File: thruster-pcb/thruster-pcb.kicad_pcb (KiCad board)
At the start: 4 copper layers, 40 x 40 mm, 103 parts, among them J1301 Connector_USB_C_Receptacle, J301 Molex_Pico-SPOX_Horizontal, J302 Molex_Pico-Lock-PLUS_Vertical, J401 Molex_Pico-SPOX_Horizontal, J402 Molex_Pico-Clasp_Horizontal, M301 Fan_5VDC_25x25x8mm, Q301 MOSFET-N-CH, SW1301 Switch_Tactile_SPST-NO_SMT_Si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, U1001 BUK7D36-60EX, U1101 BUK7D36-60EX, U1201 BUK7D36-60EX, U1301 Linear_3.3V_1A, U1302 MCU_RP2040, U1303 Memory_Flash_W25Q128JVZPIQ, U301 Switching_5V_500mA, U302 Linear_3.3V_1A, U401 TMC5160A-WA, U402 MAX6816, U501 BUK7D36-60EX, U601 BUK7D36-60EX, U701 BUK7D36-60EX, U801 BUK7D36-60EX, U901 BUK7D36-60EX, X401 16MHz, Y1301 Crystal_12MHz

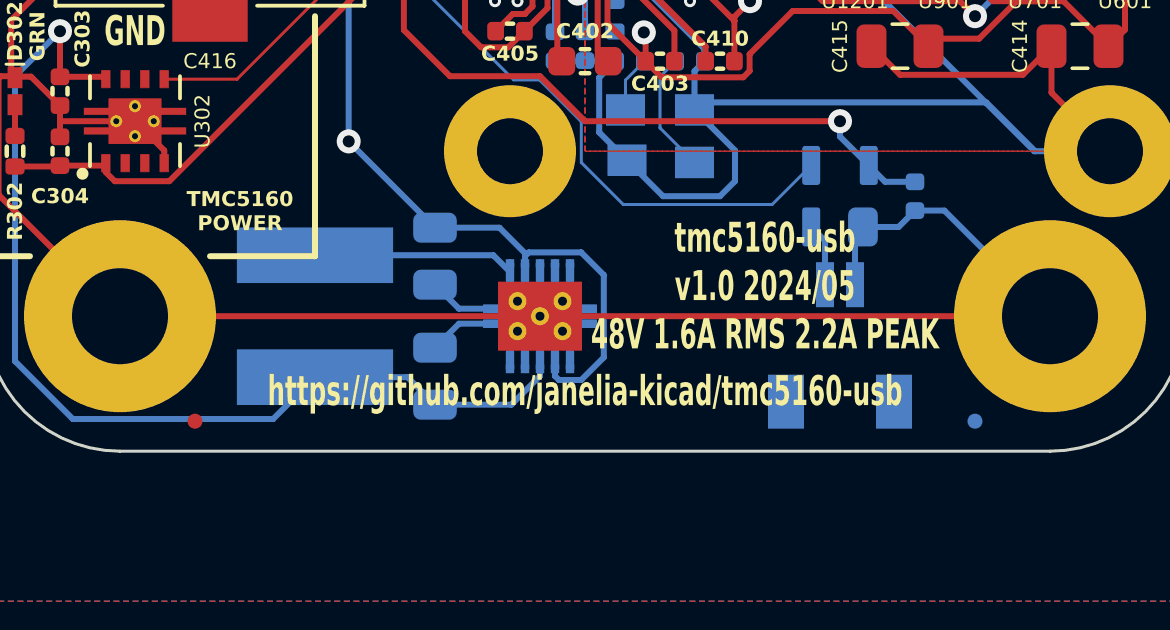
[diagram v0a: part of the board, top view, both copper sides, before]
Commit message: tmc5160-usb -> thruster-pcb
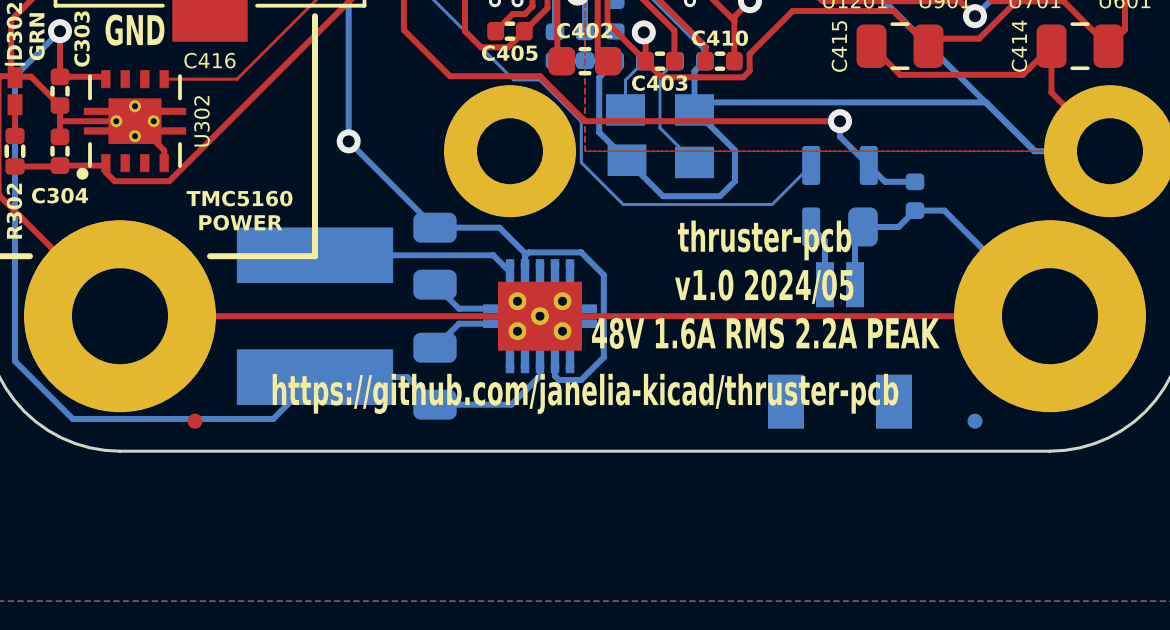
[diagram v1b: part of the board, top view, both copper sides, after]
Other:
- board text added: "https://github.com/janelia-kicad/thruster-pcb"
- board text added: "thruster-pcb v1.0 2024/05 48V 1.6A RMS 2.2A PEAK"
- board text removed: "https://github.com/janelia-kicad/tmc5160-usb"
- board text removed: "tmc5160-usb v1.0 2024/05 48V 1.6A RMS 2.2A PEAK"
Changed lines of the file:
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@@
   (paper "A4")
   (title_block
-    (title "tmc5160-usb")
+    (title "thruster-pcb")
     (date "2024-05-08")
     (rev "1.0")
@@
     (effects (font (size 1 0.6) (thickness 0.15) bold))
   )
-  (gr_text "tmc5160-usb\nv1.0 2024/05\n48V 1.6A RMS 2.2A PEAK" (at 158.4 116.1) (layer "F.SilkS")
+  (gr_text "thruster-pcb\nv1.0 2024/05\n48V 1.6A RMS 2.2A PEAK" (at 158.4 116.1) (layer "F.SilkS")
     (effects (font (size 1 0.6) (thickness 0.15) bold))
   )
-  (gr_text "https://github.com/janelia-kicad/tmc5160-usb" (at 152.4 119.6) (layer "F.SilkS")
+  (gr_text "https://github.com/janelia-kicad/thruster-pcb" (at 152.4 119.6) (layer "F.SilkS")
     (effects (font (size 1 0.6) (thickness 0.15) bold))
   )

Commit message: Add reference files
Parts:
- removed C1301, C1302, C303, C304, C305: 1uF_25V, Janelia:C_0402_1005Metric
- removed C1303, C1311: 1uF_35V, Janelia:C_0402_1005Metric
- removed C1304, C1305, C1306, C1307, C1308, C1309, C1310, C1312, C1313, C1314, C401, C403, C404, C408, C413, C417: 0.1uF_100V, Janelia:C_0402_1005Metric
- removed C1315, C1316: 15pF_25V, Janelia:C_0402_1005Metric
- removed C301, C414, C415: 2.2uF_100V, Janelia:C_0805_2012Metric
- removed C302: 47uF_10V, Janelia:C_0805_2012Metric
- removed C402: 22nF_100V, Janelia:C_0603_1608Metric
- removed C405: 0.47uF_35V, Janelia:C_0402_1005Metric
- removed C406, C407: 2.2uF_35V, Janelia:C_0402_1005Metric
- removed C409, C410, C411, C412: 0.22uF_25V, Janelia:C_0402_1005Metric
- removed C416: 220uF_63V, Janelia:CP_Hybrid_EEHZS1H221V
- removed D1301, D1302: D_SCHOTTKY_40V_2A, Janelia:CR_DSN2_152AB-C_OSI
- removed D301: LED_RED, Janelia:LED_0402-1005_KNB
- removed D302: LED_GRN, Janelia:LED_0402-1005_KNB
- removed D303: LED_YEL, Janelia:LED_0402-1005_KNB
- removed D401: D_Zener_48V_2.6A, Janelia:SMFSeries_LTF
- removed FID201, FID202, FID203, FID204: FIDUCIAL_0.5mm_MASK1mm, Janelia:FIDUCIAL_0.5mm_Mask1mm
- removed H201, H202, H203, H204: MountingHole_M3_Pad, Janelia:MountingHole_3.2mm_M3_Pad
- removed J1301: Connector_USB_C_Receptacle, Janelia:USB_C_Receptacle_Amphenol_10152803-00011LF
- removed J301: Molex_Pico-SPOX_Horizontal, Janelia:Molex_Pico-SPOX-87438_1x02-P1.5mm_Horizontal
- removed J302: Molex_Pico-Lock-PLUS_Vertical, Janelia:Molex_Micro-Lock-PLUS-505568_1x02_P1.25mm_Vertical
- removed J401: Molex_Pico-SPOX_Horizontal, Janelia:Molex_Pico-SPOX-87438_1x04-P1.5mm_Horizontal
- removed J402: Molex_Pico-Clasp_Horizontal, Janelia:Molex_Pico-Clasp-501568_1x02_P1mm_Horizontal
- removed L301: 150uH_553mA, Janelia:IND_CB_SD25
- removed M301: Fan_5VDC_25x25x8mm, Janelia:FAN_5VDC_25x25x8mm
- removed Q301: MOSFET-N-CH, Janelia:XFDFN-3
- removed R1001, R1101, R1201, R501, R601, R701, R801, R901: 15, Janelia:R_0402_1005Metric
- removed R1301: 10.0k, Janelia:R_0402_1005Metric
- removed R1302, R1303: 5.1k, Janelia:R_0402_1005Metric
- removed R1304, R1305: 27, Janelia:R_0402_1005Metric
- removed R1306, R1307: 1k, Janelia:R_0402_1005Metric
- removed R301: 2.32k, Janelia:R_0805_2012Metric
- removed R302: 64.9, Janelia:R_0402_1005Metric
- removed R303: 249, Janelia:R_0402_1005Metric
- removed R401: 2.2, Janelia:R_0402_1005Metric
- removed R402, R403, R406, R407: 47, Janelia:R_0402_1005Metric
- removed R404, R405: 0.15, Janelia:R_1206_3216Metric
- removed SW1301: Switch_Tactile_SPST-NO_SMT_Side, Janelia:SMT_1045822_WRE
- removed U1001, U1101, U1201, U501, U601, U701, U801, U901: BUK7D36-60EX, Janelia:BUK7D3660EX_NEX
- removed U1301, U302: Linear_3.3V_1A, Janelia:TPS737Q1
- removed U1302: MCU_RP2040, Janelia:QFN-56-1EP_7x7mm_P0.4mm_EP3.2x3.2mm
- removed U1303: Memory_Flash_W25Q128JVZPIQ, Janelia:WSON-8-1EP_6x5mm_P1.27mm_EP3.4x4.3mm
- removed U301: Switching_5V_500mA, Janelia:Texas_S-PVSON-N10_ThermalVias
- removed U401: TMC5160A-WA, Janelia:21-100593_ADI
- removed U402: MAX6816, Janelia:SOT192P237X122-4N
- removed X401: 16MHz, Janelia:OSC_ECS-2520S33-160-FN-TR
- removed Y1301: Crystal_12MHz, Janelia:Crystal_SMD_Abracon_ABM8-4Pin_3.2x2.5mm
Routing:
- net /GND: track 474.9 -> 0.00 mm, vias 6 -> 0
- net /VM: track 133.3 -> 0.00 mm, vias 4 -> 0
- net /rp2040/+3.3V: track 87.1 -> 0.00 mm, vias 4 -> 0
- net /+5V: track 81.3 -> 0.00 mm, vias 3 -> 0
- net /VIO: track 56.5 -> 0.00 mm, vias 1 -> 0
- net /tmc5160/BMA1: track 39.3 -> 0.00 mm, vias 2 -> 0
- net /tmc5160/SRA: track 37.6 -> 0.00 mm
- net /tmc5160/BMB2: track 33.1 -> 0.00 mm, vias 2 -> 0
- net /tmc5160/BMA2: track 32.7 -> 0.00 mm, vias 3 -> 0
- net /tmc5160/SRB: track 32.5 -> 0.00 mm
- net /tmc5160/REFL_DEBOUNCED: track 28.1 -> 0.00 mm, vias 1 -> 0
- net /tmc5160/BMB1: track 27.4 -> 0.00 mm, vias 2 -> 0
- net /tmc5160/VCC: track 21.8 -> 0.00 mm, vias 2 -> 0
- net /rp2040/+1.1V: track 20.7 -> 0.00 mm
- net /tmc5160/LA1: track 20.6 -> 0.00 mm, vias 2 -> 0
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- removed copper zone on B.Cu, net /GND
- removed copper zone on F.Cu, net /GND
- removed copper zone on In1.Cu, net /GND
- removed copper zone on F.Cu, net /VM
- removed copper zone on In2.Cu, net /VM
- removed copper zone on B.Cu, net /rp2040/+1.1V
- removed copper zone on B.Cu, net /rp2040/+3.3V
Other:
- board text removed: "+"
- board text removed: "-"
- board text removed: "48V"
- board text removed: "A1"
- board text removed: "A2"
- board text removed: "B1"
- board text removed: "B2"
- board text removed: "BOOTSEL"
- board text removed: "FAN"
- board text removed: "GND"
- board text removed: "GRN"
- board text removed: "Molex 0874380243"
- board text removed: "Molex 0874380443"
- board text removed: "Molex 5015680207"
- board text removed: "Molex 5055680281 Fan 255M"
- board text removed: "RED"
- board text removed: "REFL"
- board text removed: "TMC5160 POWER"
- board text removed: "USB-C"
- board text removed: "YEL"
- board text removed: "https://github.com/janelia-kicad/thruster-pcb"
- board text removed: "thruster-pcb v1.0 2024/05 48V 1.6A RMS 2.2A PEAK"

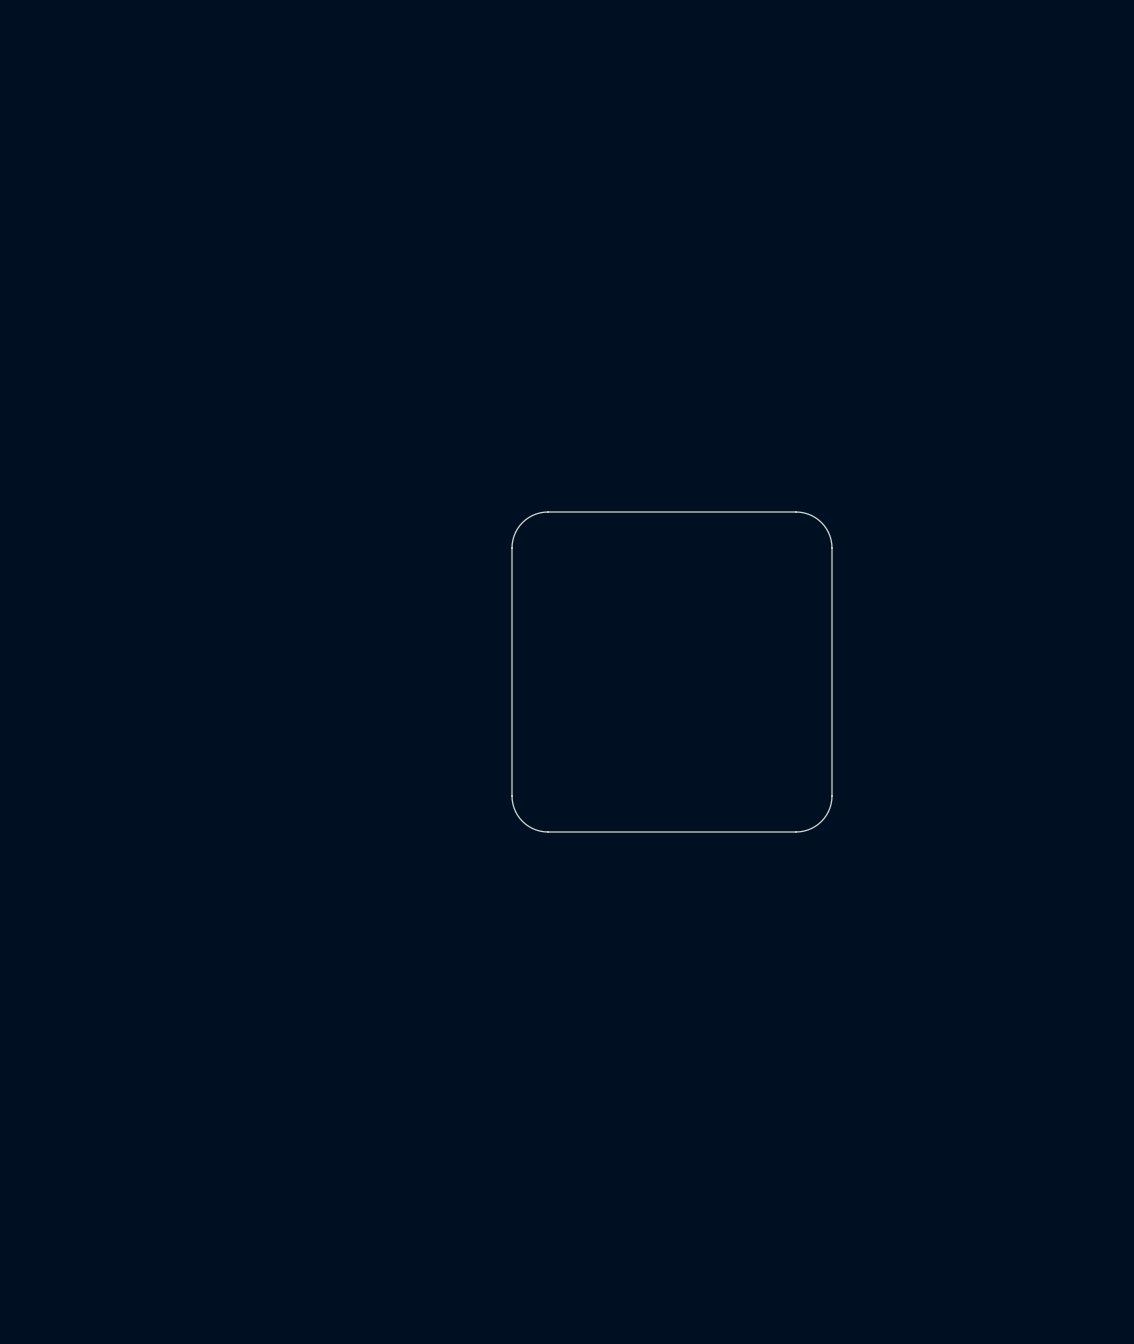
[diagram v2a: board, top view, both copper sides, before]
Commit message: Use PCA9685 and nRF52
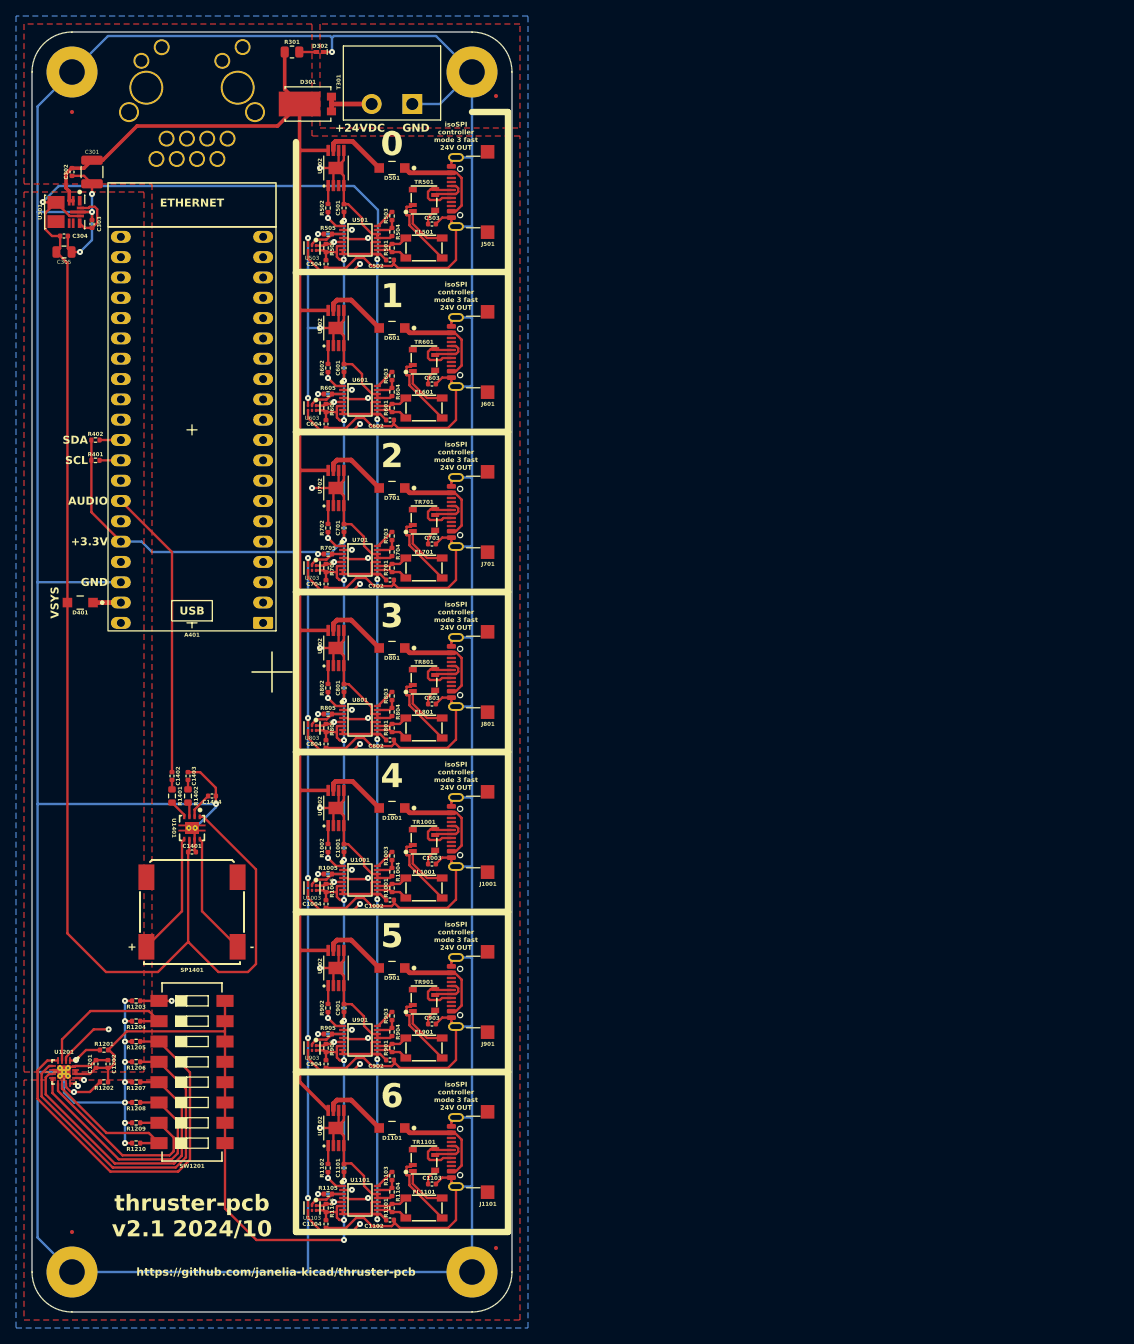
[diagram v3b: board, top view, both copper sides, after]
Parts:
- added A401: PICO_W5500_EVB, Janelia:Pico-W5500-EVB_Header_Holes, F.Cu at (92.4, 95.5)
- added C1001: 0.1uF_100V, Janelia:C_0402_1005Metric, F.Cu at (111.4, 123.6)
- added C1002: 0.1uF_100V, Janelia:C_0402_1005Metric, F.Cu at (117.2, 130.1)
- added C1003: 27pF_50V, Janelia:C_0402_1005Metric, F.Cu at (122.4, 125.6)
- added C1004: 0.1uF_100V, Janelia:C_0402_1005Metric, F.Cu at (109.2, 130.6)
- added C1101: 0.1uF_100V, Janelia:C_0402_1005Metric, F.Cu at (111.4, 163.6)
- added C1102: 0.1uF_100V, Janelia:C_0402_1005Metric, F.Cu at (117.2, 170.1)
- added C1103: 27pF_50V, Janelia:C_0402_1005Metric, F.Cu at (122.4, 165.6)
- added C1104: 0.1uF_100V, Janelia:C_0402_1005Metric, F.Cu at (109.2, 170.6)
- added C1201: 0.1uF_100V, Janelia:C_0402_1005Metric, F.Cu at (80.4, 150.6)
- added C1202: 0.1uF_100V, Janelia:C_0402_1005Metric, F.Cu at (81.9, 150.6)
- added C1401: 1uF_35V, Janelia:C_0402_1005Metric, F.Cu at (92.4, 124.1)
- added C1402: 0.22uF_25V, Janelia:C_0402_1005Metric, F.Cu at (89.9, 114.6)
- added C1403: 0.22uF_25V, Janelia:C_0402_1005Metric, F.Cu at (91.9, 114.6)
- added C1404: 0.22uF_25V, Janelia:C_0402_1005Metric, F.Cu at (94.9, 117.1)
- added C301: 3.3uF_50V, Janelia:C_1210_3225Metric, F.Cu at (79.9, 39.1)
- added C302: 0.1uF_100V, Janelia:C_0402_1005Metric, F.Cu at (77.4, 39.1)
- added C303: 1uF_25V, Janelia:C_0402_1005Metric, F.Cu at (79.9, 45.6)
- added C304: 1uF_25V, Janelia:C_0402_1005Metric, F.Cu at (76.4, 47.1)
- added C305: 47uF_10V, Janelia:C_0805_2012Metric, F.Cu at (76.4, 49.1)
- added C501: 0.1uF_100V, Janelia:C_0402_1005Metric, F.Cu at (111.4, 43.6)
- added C502: 0.1uF_100V, Janelia:C_0402_1005Metric, F.Cu at (117.2, 50.1)
- added C503: 27pF_50V, Janelia:C_0402_1005Metric, F.Cu at (122.4, 45.6)
- added C504: 0.1uF_100V, Janelia:C_0402_1005Metric, F.Cu at (109.2, 50.6)
- added C601: 0.1uF_100V, Janelia:C_0402_1005Metric, F.Cu at (111.4, 63.6)
- added C602: 0.1uF_100V, Janelia:C_0402_1005Metric, F.Cu at (117.2, 70.1)
- added C603: 27pF_50V, Janelia:C_0402_1005Metric, F.Cu at (122.4, 65.6)
- added C604: 0.1uF_100V, Janelia:C_0402_1005Metric, F.Cu at (109.2, 70.6)
- added C701: 0.1uF_100V, Janelia:C_0402_1005Metric, F.Cu at (111.4, 83.6)
- added C702: 0.1uF_100V, Janelia:C_0402_1005Metric, F.Cu at (117.2, 90.1)
- added C703: 27pF_50V, Janelia:C_0402_1005Metric, F.Cu at (122.4, 85.6)
- added C704: 0.1uF_100V, Janelia:C_0402_1005Metric, F.Cu at (109.2, 90.6)
- added C801: 0.1uF_100V, Janelia:C_0402_1005Metric, F.Cu at (111.4, 103.6)
- added C802: 0.1uF_100V, Janelia:C_0402_1005Metric, F.Cu at (117.2, 110.1)
- added C803: 27pF_50V, Janelia:C_0402_1005Metric, F.Cu at (122.4, 105.6)
- added C804: 0.1uF_100V, Janelia:C_0402_1005Metric, F.Cu at (109.2, 110.6)
- added C901: 0.1uF_100V, Janelia:C_0402_1005Metric, F.Cu at (111.4, 143.6)
- added C902: 0.1uF_100V, Janelia:C_0402_1005Metric, F.Cu at (117.2, 150.1)
- added C903: 27pF_50V, Janelia:C_0402_1005Metric, F.Cu at (122.4, 145.6)
- added C904: 0.1uF_100V, Janelia:C_0402_1005Metric, F.Cu at (109.2, 150.6)
- added D1001: D_SCHOTTKY_20V_1A, Janelia:SOD-123FL, F.Cu at (117.4, 118.6)
- added D1101: D_SCHOTTKY_20V_1A, Janelia:SOD-123FL, F.Cu at (117.4, 158.6)
- added D301: D_50V_15A, Janelia:POWERDI5_DIO, F.Cu at (106.9, 30.6)
- added D302: LED_RED, Janelia:LED_0402-1005_KNB, F.Cu at (108.4, 24.1)
- added D401: D_SCHOTTKY_20V_1A, Janelia:SOD-123FL, F.Cu at (78.4, 92.9)
- added D501: D_SCHOTTKY_20V_1A, Janelia:SOD-123FL, F.Cu at (117.4, 38.6)
- added D601: D_SCHOTTKY_20V_1A, Janelia:SOD-123FL, F.Cu at (117.4, 58.6)
- added D701: D_SCHOTTKY_20V_1A, Janelia:SOD-123FL, F.Cu at (117.4, 78.6)
- added D801: D_SCHOTTKY_20V_1A, Janelia:SOD-123FL, F.Cu at (117.4, 98.6)
- added D901: D_SCHOTTKY_20V_1A, Janelia:SOD-123FL, F.Cu at (117.4, 138.6)
- added FID201: FIDUCIAL_0.5mm_MASK1mm, Janelia:FIDUCIAL_0.5mm_Mask1mm, F.Cu at (77.4, 31.6)
- added FID202: FIDUCIAL_0.5mm_MASK1mm, Janelia:FIDUCIAL_0.5mm_Mask1mm, F.Cu at (130.4, 29.6)
- added FID203: FIDUCIAL_0.5mm_MASK1mm, Janelia:FIDUCIAL_0.5mm_Mask1mm, F.Cu at (130.4, 173.6)
- added FID204: FIDUCIAL_0.5mm_MASK1mm, Janelia:FIDUCIAL_0.5mm_Mask1mm, F.Cu at (77.4, 171.6)
- added FL1001: Choke_CMF_ACT45B-220-2P, Janelia:SMD_0-2P-TL003_TDK-L, F.Cu at (121.4, 128.6)
- added FL1101: Choke_CMF_ACT45B-220-2P, Janelia:SMD_0-2P-TL003_TDK-L, F.Cu at (121.4, 168.6)
- added FL501: Choke_CMF_ACT45B-220-2P, Janelia:SMD_0-2P-TL003_TDK-L, F.Cu at (121.4, 48.6)
- added FL601: Choke_CMF_ACT45B-220-2P, Janelia:SMD_0-2P-TL003_TDK-L, F.Cu at (121.4, 68.6)
- added FL701: Choke_CMF_ACT45B-220-2P, Janelia:SMD_0-2P-TL003_TDK-L, F.Cu at (121.4, 88.6)
- added FL801: Choke_CMF_ACT45B-220-2P, Janelia:SMD_0-2P-TL003_TDK-L, F.Cu at (121.4, 108.6)
- added FL901: Choke_CMF_ACT45B-220-2P, Janelia:SMD_0-2P-TL003_TDK-L, F.Cu at (121.4, 148.6)
- added H201: MountingHole_M3_Pad, Janelia:MountingHole_3.2mm_M3_Pad, F.Cu at (77.4, 26.6)
- added H202: MountingHole_M3_Pad, Janelia:MountingHole_3.2mm_M3_Pad, F.Cu at (127.4, 26.6)
- added H203: MountingHole_M3_Pad, Janelia:MountingHole_3.2mm_M3_Pad, F.Cu at (127.4, 176.6)
- added H204: MountingHole_M3_Pad, Janelia:MountingHole_3.2mm_M3_Pad, F.Cu at (77.4, 176.6)
- added J1001: Connector_USB_C_Receptacle_USB2.0_16P_GT-USB-7047C, Janelia:USB_C_Receptacle_GT-USB-7047C_16P_TopMnt_Horizontal, F.Cu at (125.4, 121.6)
- added J1101: Connector_USB_C_Receptacle_USB2.0_16P_GT-USB-7047C, Janelia:USB_C_Receptacle_GT-USB-7047C_16P_TopMnt_Horizontal, F.Cu at (125.4, 161.6)
- added J501: Connector_USB_C_Receptacle_USB2.0_16P_GT-USB-7047C, Janelia:USB_C_Receptacle_GT-USB-7047C_16P_TopMnt_Horizontal, F.Cu at (125.4, 41.6)
- added J601: Connector_USB_C_Receptacle_USB2.0_16P_GT-USB-7047C, Janelia:USB_C_Receptacle_GT-USB-7047C_16P_TopMnt_Horizontal, F.Cu at (125.4, 61.6)
- added J701: Connector_USB_C_Receptacle_USB2.0_16P_GT-USB-7047C, Janelia:USB_C_Receptacle_GT-USB-7047C_16P_TopMnt_Horizontal, F.Cu at (125.4, 81.6)
- added J801: Connector_USB_C_Receptacle_USB2.0_16P_GT-USB-7047C, Janelia:USB_C_Receptacle_GT-USB-7047C_16P_TopMnt_Horizontal, F.Cu at (125.4, 101.6)
- added J901: Connector_USB_C_Receptacle_USB2.0_16P_GT-USB-7047C, Janelia:USB_C_Receptacle_GT-USB-7047C_16P_TopMnt_Horizontal, F.Cu at (125.4, 141.6)
- added R1001: 100, Janelia:R_0402_1005Metric, F.Cu at (117.4, 128.6)
- added R1002: 4.7k, Janelia:R_0402_1005Metric, F.Cu at (109.4, 123.6)
- added R1003: 1.4k, Janelia:R_0402_1005Metric, F.Cu at (117.4, 124.6)
- added R1004: 604, Janelia:R_0402_1005Metric, F.Cu at (117.4, 126.6)
- added R1005: 1.8k, Janelia:R_0402_1005Metric, F.Cu at (109.4, 126.8)
- added R1006: 1.8k, Janelia:R_0402_1005Metric, F.Cu at (109.2, 128.6)
- added R1101: 100, Janelia:R_0402_1005Metric, F.Cu at (117.4, 168.6)
- added R1102: 4.7k, Janelia:R_0402_1005Metric, F.Cu at (109.4, 163.6)
- added R1103: 1.4k, Janelia:R_0402_1005Metric, F.Cu at (117.4, 164.6)
- added R1104: 604, Janelia:R_0402_1005Metric, F.Cu at (117.4, 166.6)
- added R1105: 1.8k, Janelia:R_0402_1005Metric, F.Cu at (109.4, 166.8)
- added R1106: 1.8k, Janelia:R_0402_1005Metric, F.Cu at (109.2, 168.6)
- added R1201: 10.0k, Janelia:R_0402_1005Metric, F.Cu at (81.4, 148.8)
- added R1202: 10.0k, Janelia:R_0402_1005Metric, F.Cu at (81.4, 152.8)
- added R1203: 10.0k, Janelia:R_0402_1005Metric, F.Cu at (85.4, 142.7)
- added R1204: 10.0k, Janelia:R_0402_1005Metric, F.Cu at (85.4, 145.2)
- added R1205: 10.0k, Janelia:R_0402_1005Metric, F.Cu at (85.4, 147.8)
- added R1206: 10.0k, Janelia:R_0402_1005Metric, F.Cu at (85.4, 150.3)
- added R1207: 10.0k, Janelia:R_0402_1005Metric, F.Cu at (85.4, 152.9)
- added R1208: 10.0k, Janelia:R_0402_1005Metric, F.Cu at (85.4, 155.4)
- added R1209: 10.0k, Janelia:R_0402_1005Metric, F.Cu at (85.4, 157.9)
- added R1210: 10.0k, Janelia:R_0402_1005Metric, F.Cu at (85.4, 160.5)
- added R1401: 40k, Janelia:R_0603_1608Metric, F.Cu at (89.9, 117.1)
- added R1402: 40k, Janelia:R_0603_1608Metric, F.Cu at (91.9, 117.1)
- added R301: 2.32k, Janelia:R_0805_2012Metric, F.Cu at (104.9, 24.1)
- added R401: 1.8k, Janelia:R_0402_1005Metric, F.Cu at (80.3, 75.1)
- added R402: 1.8k, Janelia:R_0402_1005Metric, F.Cu at (80.3, 72.6)
- added R501: 100, Janelia:R_0402_1005Metric, F.Cu at (117.4, 48.6)
- added R502: 4.7k, Janelia:R_0402_1005Metric, F.Cu at (109.4, 43.6)
- added R503: 1.4k, Janelia:R_0402_1005Metric, F.Cu at (117.4, 44.6)
- added R504: 604, Janelia:R_0402_1005Metric, F.Cu at (117.4, 46.6)
- added R505: 1.8k, Janelia:R_0402_1005Metric, F.Cu at (109.4, 46.9)
- added R506: 1.8k, Janelia:R_0402_1005Metric, F.Cu at (109.2, 48.6)
- added R601: 100, Janelia:R_0402_1005Metric, F.Cu at (117.4, 68.6)
- added R602: 4.7k, Janelia:R_0402_1005Metric, F.Cu at (109.4, 63.6)
- added R603: 1.4k, Janelia:R_0402_1005Metric, F.Cu at (117.4, 64.6)
- added R604: 604, Janelia:R_0402_1005Metric, F.Cu at (117.4, 66.6)
- added R605: 1.8k, Janelia:R_0402_1005Metric, F.Cu at (109.4, 66.8)
- added R606: 1.8k, Janelia:R_0402_1005Metric, F.Cu at (109.2, 68.6)
- added R701: 100, Janelia:R_0402_1005Metric, F.Cu at (117.4, 88.6)
- added R702: 4.7k, Janelia:R_0402_1005Metric, F.Cu at (109.4, 83.6)
- added R703: 1.4k, Janelia:R_0402_1005Metric, F.Cu at (117.4, 84.6)
- added R704: 604, Janelia:R_0402_1005Metric, F.Cu at (117.4, 86.6)
- added R705: 1.8k, Janelia:R_0402_1005Metric, F.Cu at (109.4, 86.8)
- added R706: 1.8k, Janelia:R_0402_1005Metric, F.Cu at (109.2, 88.6)
- added R801: 100, Janelia:R_0402_1005Metric, F.Cu at (117.4, 108.6)
- added R802: 4.7k, Janelia:R_0402_1005Metric, F.Cu at (109.4, 103.6)
- added R803: 1.4k, Janelia:R_0402_1005Metric, F.Cu at (117.4, 104.6)
- added R804: 604, Janelia:R_0402_1005Metric, F.Cu at (117.4, 106.6)
- added R805: 1.8k, Janelia:R_0402_1005Metric, F.Cu at (109.4, 106.8)
- added R806: 1.8k, Janelia:R_0402_1005Metric, F.Cu at (109.2, 108.6)
- added R901: 100, Janelia:R_0402_1005Metric, F.Cu at (117.4, 148.6)
- added R902: 4.7k, Janelia:R_0402_1005Metric, F.Cu at (109.4, 143.6)
- added R903: 1.4k, Janelia:R_0402_1005Metric, F.Cu at (117.4, 144.6)
- added R904: 604, Janelia:R_0402_1005Metric, F.Cu at (117.4, 146.6)
- added R905: 1.8k, Janelia:R_0402_1005Metric, F.Cu at (109.4, 146.8)
- added R906: 1.8k, Janelia:R_0402_1005Metric, F.Cu at (109.2, 148.6)
- added SP1401: Speaker_13x13mm_8Ohm_700mW, Janelia:Speaker_13x13mm_KLJ-01304T-08R07W, F.Cu at (92.4, 131.6)
- added SW1201: SW_DIP_x08_SDA08H1SBDR, Janelia:SW_DIP_SPSTx08_Slide_SDA08H1SBDR, F.Cu at (92.4, 151.6)
- added T301: TERM_BLK_HDR_2POS_90DEG_0.2IN, Janelia:PHOENIX_1757242, F.Cu at (123.5, 20.6)
- added TR1001: 1:1, Janelia:FB020G00, F.Cu at (121.4, 122.6)
- added TR1101: 1:1, Janelia:FB020G00, F.Cu at (121.4, 162.6)
- added TR501: 1:1, Janelia:FB020G00, F.Cu at (121.4, 42.6)
- added TR601: 1:1, Janelia:FB020G00, F.Cu at (121.4, 62.6)
- added TR701: 1:1, Janelia:FB020G00, F.Cu at (121.4, 82.6)
- added TR801: 1:1, Janelia:FB020G00, F.Cu at (121.4, 102.6)
- added TR901: 1:1, Janelia:FB020G00, F.Cu at (121.4, 142.6)
- added U1001: LTC6820HMS-TRPBF, Janelia:MS_05-08-1669_ADI, F.Cu at (113.4, 127.6)
- added U1002: TPS1H200AQDGNRQ1, Janelia:SOP65P490X110-9N, F.Cu at (110.4, 118.6)
- added U1003: Buffer_74LVC1G125DRYR, Janelia:DRY6, F.Cu at (107.4, 128.6)
- added U1101: LTC6820HMS-TRPBF, Janelia:MS_05-08-1669_ADI, F.Cu at (113.4, 167.6)
- added U1102: TPS1H200AQDGNRQ1, Janelia:SOP65P490X110-9N, F.Cu at (110.4, 158.6)
- added U1103: Buffer_74LVC1G125DRYR, Janelia:DRY6, F.Cu at (107.4, 168.6)
- added U1201: TCA6408ARGTR, Janelia:QFN50P300X300X100-17N, F.Cu at (76.4, 151.6)
- added U1401: TPA6204A1DRBR, Janelia:DRB8_1P75X1P5, F.Cu at (92.4, 121.1)
- added U301: TPSM365R6V5RDNR, Janelia:RDN0011A-MFG, F.Cu at (76.4, 44.1)
- added U501: LTC6820HMS-TRPBF, Janelia:MS_05-08-1669_ADI, F.Cu at (113.4, 47.6)
- added U502: TPS1H200AQDGNRQ1, Janelia:SOP65P490X110-9N, F.Cu at (110.4, 38.6)
- added U503: Buffer_74LVC1G125DRYR, Janelia:DRY6, F.Cu at (107.4, 48.6)
- added U601: LTC6820HMS-TRPBF, Janelia:MS_05-08-1669_ADI, F.Cu at (113.4, 67.6)
- added U602: TPS1H200AQDGNRQ1, Janelia:SOP65P490X110-9N, F.Cu at (110.4, 58.6)
- added U603: Buffer_74LVC1G125DRYR, Janelia:DRY6, F.Cu at (107.4, 68.6)
- added U701: LTC6820HMS-TRPBF, Janelia:MS_05-08-1669_ADI, F.Cu at (113.4, 87.6)
- added U702: TPS1H200AQDGNRQ1, Janelia:SOP65P490X110-9N, F.Cu at (110.4, 78.6)
- added U703: Buffer_74LVC1G125DRYR, Janelia:DRY6, F.Cu at (107.4, 88.6)
- added U801: LTC6820HMS-TRPBF, Janelia:MS_05-08-1669_ADI, F.Cu at (113.4, 107.6)
- added U802: TPS1H200AQDGNRQ1, Janelia:SOP65P490X110-9N, F.Cu at (110.4, 98.6)
- added U803: Buffer_74LVC1G125DRYR, Janelia:DRY6, F.Cu at (107.4, 108.6)
- added U901: LTC6820HMS-TRPBF, Janelia:MS_05-08-1669_ADI, F.Cu at (113.4, 147.6)
- added U902: TPS1H200AQDGNRQ1, Janelia:SOP65P490X110-9N, F.Cu at (110.4, 138.6)
- added U903: Buffer_74LVC1G125DRYR, Janelia:DRY6, F.Cu at (107.4, 148.6)
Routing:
- net /GND: track 0.00 -> 1037.9 mm, vias 0 -> 27
- net /+5V: track 0.00 -> 401.7 mm, vias 0 -> 8
- net /+3.3V: track 0.00 -> 319.9 mm, vias 0 -> 22
- net /PRISM_CIPO: track 0.00 -> 195.6 mm, vias 0 -> 7
- net /VAA: track 0.00 -> 193.0 mm
- net /PRISM_SCK: track 0.00 -> 157.1 mm, vias 0 -> 7
- net /~{PRISMS_RESET}: track 0.00 -> 150.0 mm, vias 0 -> 7
- net /PRISM_COPI: track 0.00 -> 143.6 mm, vias 0 -> 7
- net /~{PRISM_CS_6}: track 0.00 -> 89.7 mm, vias 0 -> 1
- net /SDA: track 0.00 -> 86.4 mm, vias 0 -> 1
- net /SCL: track 0.00 -> 84.9 mm, vias 0 -> 1
- net /~{ADDRESS_INT}: track 0.00 -> 78.9 mm, vias 0 -> 1
- net /~{PRISM_CS_5}: track 0.00 -> 72.3 mm, vias 0 -> 1
- net /~{ADDRESS_RESET}: track 0.00 -> 68.6 mm, vias 0 -> 1
- net /~{PRISM_CS_3}: track 0.00 -> 55.5 mm, vias 0 -> 1
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- added copper zone on F.Cu, net /+5V
- added copper zone on B.Cu, net /GND
- added copper zone on In1.Cu, net /GND
- added copper zone on In2.Cu, net /GND
- added copper zone on F.Cu, net /VAA
- added copper zone on F.Cu, net /power/VAA
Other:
- board size 40 x 40 mm -> 60 x 160 mm
- board text added: "+24VDC"
- board text added: "+3.3V"
- board text added: "0"
- board text added: "1"
- board text added: "2"
- board text added: "3"
- board text added: "4"
- board text added: "5"
- board text added: "6"
- board text added: "AUDIO"
- board text added: "GND"
- board text added: "SCL"
- board text added: "SDA"
- board text added: "VSYS"
- board text added: "https://github.com/janelia-kicad/thruster-pcb"
- board text added: "isoSPI controller mode 3 fast 24V OUT"
- board text added: "thruster-pcb v2.1 2024/10"
